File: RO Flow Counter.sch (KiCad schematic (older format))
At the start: 27 parts, among them J7 Conn_01x02, J8 Conn_01x04, K1 G5Q-1A, Q1 BC807, Q2 BC807, Q3 2N7002E

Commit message: fix rotary encoder, i2c pullup resistors, reset button placement
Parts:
- J8: value Conn_01x04 -> Programming; footprint Connector_PinHeader_2.54mm:PinHeader_1x04_P2.54mm_Vertical -> Connector_PinHeader_2.54mm:PinHeader_1x05_P2.54mm_Vertical; symbol Connector_Generic:Conn_01x04 -> Connector_Generic:Conn_01x05
- R1, R2: value 1M -> 10k
- R20: value 1k -> 10k
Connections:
- net GND: now also J8.5 (Pin_5); no longer J8.4 (Pin_4)
- new net mcu/reset: J8.4 (Pin_4)
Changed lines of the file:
@@
 F14 "SDA" B R 6675 3775 50
 F15 "RESET_LCD" O R 6675 4075 50
+F16 "reset" I R 6675 5825 50
 $EndSheet
 Wire Wire Line
@@
 P 4200 5150
 F 0 "R2" V 3993 5150 50  0000 C CNN
-F 1 "1M" V 4084 5150 50  0000 C CNN
+F 1 "10k" V 4084 5150 50  0000 C CNN
 F 2 "Resistor_SMD:R_0402_1005Metric" V 4130 5150 50  0001 C CNN
 F 3 "~" H 4200 5150 50  0001 C CNN
@@
 P 4200 4550
 F 0 "R1" V 3993 4550 50  0000 C CNN
-F 1 "1M" V 4084 4550 50  0000 C CNN
+F 1 "10k" V 4084 4550 50  0000 C CNN
 F 2 "Resistor_SMD:R_0402_1005Metric" V 4130 4550 50  0001 C CNN
 F 3 "~" H 4200 4550 50  0001 C CNN
@@
 $EndComp
 $Comp
-L Connector_Generic:Conn_01x04 J8
+L Connector_Generic:Conn_01x05 J8
 U 1 1 62E41334
-P 7750 5625
-F 0 "J8" H 7830 5617 50  0000 L CNN
-F 1 "Conn_01x04" H 7830 5526 50  0000 L CNN
-F 2 "Connector_PinHeader_2.54mm:PinHeader_1x04_P2.54mm_Vertical" H 7750 5625 50  0001 C CNN
-F 3 "~" H 7750 5625 50  0001 C CNN
-	1    7750 5625
+P 7750 5725
+F 0 "J8" H 7830 5717 50  0000 L CNN
+F 1 "Programming" H 7830 5626 50  0000 L CNN
+F 2 "Connector_PinHeader_2.54mm:PinHeader_1x05_P2.54mm_Vertical" H 7750 5725 50  0001 C CNN
+F 3 "~" H 7750 5725 50  0001 C CNN
+	1    7750 5725
 	1    0    0    -1
 $EndComp
@@
 	7225 5525 7225 5300
 Wire Wire Line
-	7550 5825 7225 5825
-Wire Wire Line
-	7225 5825 7225 6050
+	7550 5925 7225 5925
+Wire Wire Line
+	7225 5925 7225 6150
 $Comp
 L power:GND #PWR031
 U 1 1 62E44ED0
-P 7225 6050
-F 0 "#PWR031" H 7225 5800 50  0001 C CNN
-F 1 "GND" H 7230 5877 50  0000 C CNN
-F 2 "" H 7225 6050 50  0001 C CNN
-F 3 "" H 7225 6050 50  0001 C CNN
-	1    7225 6050
+P 7225 6150
+F 0 "#PWR031" H 7225 5900 50  0001 C CNN
+F 1 "GND" H 7230 5977 50  0000 C CNN
+F 2 "" H 7225 6150 50  0001 C CNN
+F 3 "" H 7225 6150 50  0001 C CNN
+	1    7225 6150
 	1    0    0    -1
 $EndComp
@@
 P 7725 2925
 F 0 "R20" V 7518 2925 50  0000 C CNN
-F 1 "1k" V 7609 2925 50  0000 C CNN
+F 1 "10k" V 7609 2925 50  0000 C CNN
 F 2 "Resistor_SMD:R_0402_1005Metric" V 7655 2925 50  0001 C CNN
 F 3 "~" H 7725 2925 50  0001 C CNN
@@
 Wire Wire Line
 	7725 3225 8125 3225
+Wire Wire Line
+	7550 5825 6675 5825
 $EndSCHEMATC

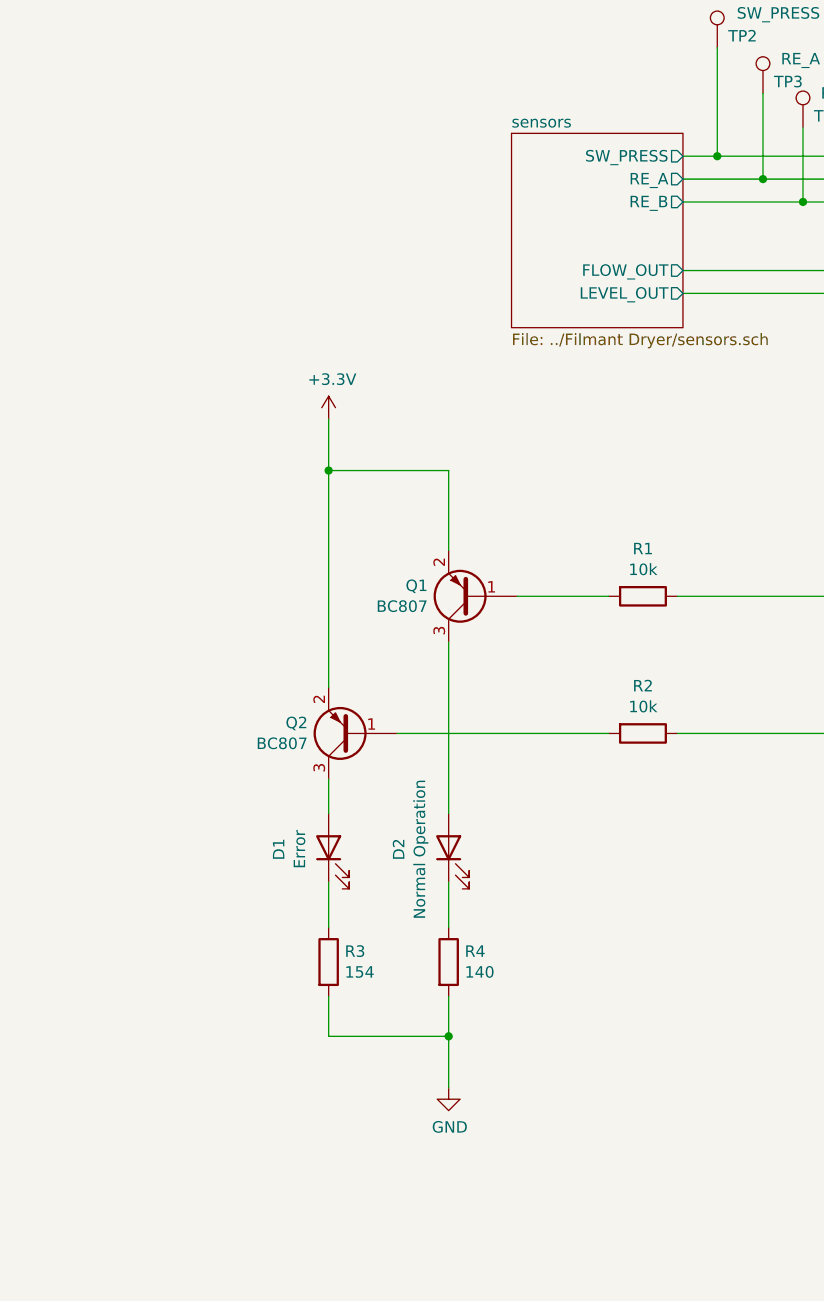
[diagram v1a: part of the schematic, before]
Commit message: use mosfet for led instead of bjt
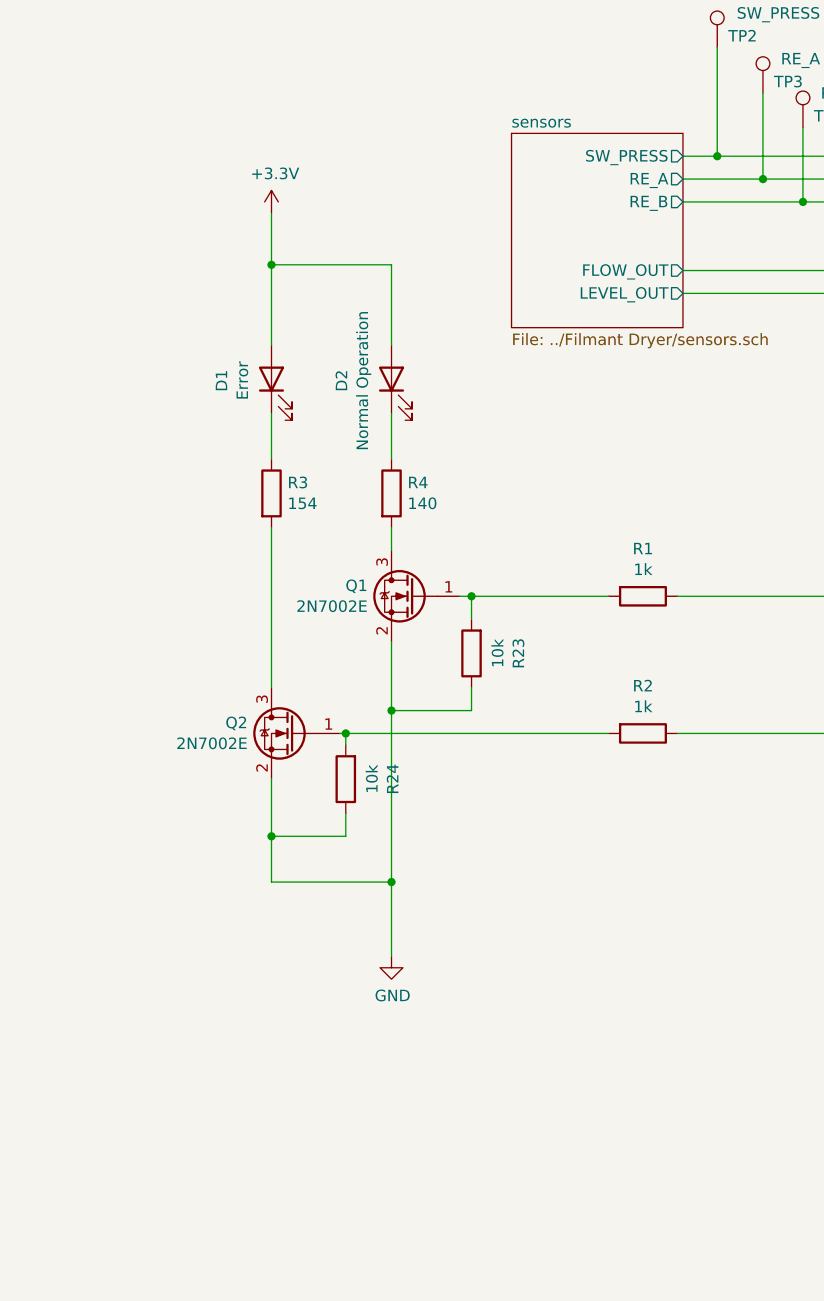
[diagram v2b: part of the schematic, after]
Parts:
- removed Q1, Q2: BC807, Package_TO_SOT_SMD:SOT-23, symbol Transistor_BJT:BC807
- added Q1, Q2: 2N7002E, Package_TO_SOT_SMD:SOT-23, symbol Transistor_FET:2N7002E
- added R23, R24: 10k, Resistor_SMD:R_0402_1005Metric, symbol Device:R
- R1, R2: value 10k -> 1k
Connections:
- net +3V3: now also D1.2 (A), D2.2 (A)
- net GND: now also Q1.2 (S), Q2.2 (S), R23.1, R24.1; no longer R3.2, R4.2
- net at R1.2: now also Q1.1 (G), R23.2
- net at R2.2: now also Q2.1 (G), R24.2
- new net: Q2.3 (D), R3.2
- new net: Q1.3 (D), R4.2
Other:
- moved on the sheet: D1, D2, R3, R4
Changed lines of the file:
@@
 L Device:LED D1
 U 1 1 62E04814
-P 2825 5650
-F 0 "D1" H 2818 5867 50  0000 C CNN
-F 1 "Error" H 2818 5776 50  0000 C CNN
-F 2 "LED_SMD:LED_0805_2012Metric" H 2825 5650 50  0001 C CNN
-F 3 "~" H 2825 5650 50  0001 C CNN
-	1    2825 5650
+P 2575 3600
+F 0 "D1" H 2568 3817 50  0000 C CNN
+F 1 "Error" H 2568 3726 50  0000 C CNN
+F 2 "LED_SMD:LED_0805_2012Metric" H 2575 3600 50  0001 C CNN
+F 3 "~" H 2575 3600 50  0001 C CNN
+	1    2575 3600
 	0    -1   -1   0
 $EndComp
@@
 L Device:LED D2
 U 1 1 62E049EE
-P 3350 5650
-F 0 "D2" H 3343 5867 50  0000 C CNN
-F 1 "Normal Operation" H 3343 5776 50  0000 C CNN
-F 2 "LED_SMD:LED_0805_2012Metric" H 3350 5650 50  0001 C CNN
-F 3 "~" H 3350 5650 50  0001 C CNN
-	1    3350 5650
+P 3100 3600
+F 0 "D2" H 3093 3817 50  0000 C CNN
+F 1 "Normal Operation" H 3093 3726 50  0000 C CNN
+F 2 "LED_SMD:LED_0805_2012Metric" H 3100 3600 50  0001 C CNN
+F 3 "~" H 3100 3600 50  0001 C CNN
+	1    3100 3600
 	0    -1   -1   0
 $EndComp
-$Comp
-L Transistor_BJT:BC807 Q1
-U 1 1 62E0B219
-P 3450 4550
-F 0 "Q1" H 3641 4504 50  0000 L CNN
-F 1 "BC807" H 3641 4595 50  0000 L CNN
-F 2 "Package_TO_SOT_SMD:SOT-23" H 3650 4475 50  0001 L CIN
-F 3 "https://www.onsemi.com/pub/Collateral/BC808-D.pdf" H 3450 4550 50  0001 L CNN
-	1    3450 4550
-	-1   0    0    1
-$EndComp
-$Comp
-L Transistor_BJT:BC807 Q2
-U 1 1 62E0CCA7
-P 2925 5150
-F 0 "Q2" H 3116 5104 50  0000 L CNN
-F 1 "BC807" H 3116 5195 50  0000 L CNN
-F 2 "Package_TO_SOT_SMD:SOT-23" H 3125 5075 50  0001 L CIN
-F 3 "https://www.onsemi.com/pub/Collateral/BC808-D.pdf" H 2925 5150 50  0001 L CNN
-	1    2925 5150
-	-1   0    0    1
-$EndComp
-Wire Wire Line
-	3350 4350 3350 4000
-Wire Wire Line
-	2825 4000 2825 4950
-Wire Wire Line
-	3350 5500 3350 4750
-Wire Wire Line
-	2825 5350 2825 5500
-Wire Wire Line
-	3350 4000 2825 4000
-Wire Wire Line
-	2825 4000 2825 3775
-Connection ~ 2825 4000
 $Comp
 L Device:R R4
 U 1 1 62E115BD
-P 3350 6150
-F 0 "R4" H 3420 6196 50  0000 L CNN
-F 1 "140" H 3420 6105 50  0000 L CNN
-F 2 "Resistor_SMD:R_0402_1005Metric" V 3280 6150 50  0001 C CNN
-F 3 "~" H 3350 6150 50  0001 C CNN
-	1    3350 6150
+P 3100 4100
+F 0 "R4" H 3170 4146 50  0000 L CNN
+F 1 "140" H 3170 4055 50  0000 L CNN
+F 2 "Resistor_SMD:R_0402_1005Metric" V 3030 4100 50  0001 C CNN
+F 3 "~" H 3100 4100 50  0001 C CNN
+	1    3100 4100
 	1    0    0    -1
 $EndComp
@@
 L Device:R R3
 U 1 1 62E11255
-P 2825 6150
-F 0 "R3" H 2895 6196 50  0000 L CNN
-F 1 "154" H 2895 6105 50  0000 L CNN
-F 2 "Resistor_SMD:R_0402_1005Metric" V 2755 6150 50  0001 C CNN
-F 3 "~" H 2825 6150 50  0001 C CNN
-	1    2825 6150
-	1    0    0    -1
-$EndComp
-Wire Wire Line
-	2825 6000 2825 5800
-Wire Wire Line
-	2825 6300 2825 6475
-Wire Wire Line
-	2825 6475 3350 6475
-Wire Wire Line
-	3350 6475 3350 6300
-Wire Wire Line
-	3350 6475 3350 6700
-Connection ~ 3350 6475
-Wire Wire Line
-	3125 5150 4050 5150
-Wire Wire Line
-	3650 4550 4050 4550
+P 2575 4100
+F 0 "R3" H 2645 4146 50  0000 L CNN
+F 1 "154" H 2645 4055 50  0000 L CNN
+F 2 "Resistor_SMD:R_0402_1005Metric" V 2505 4100 50  0001 C CNN
+F 3 "~" H 2575 4100 50  0001 C CNN
+	1    2575 4100
+	1    0    0    -1
+$EndComp
+Wire Wire Line
+	2575 3950 2575 3750
 $Comp
 L Device:R R2
@@
 P 4200 5150
 F 0 "R2" V 3993 5150 50  0000 C CNN
-F 1 "10k" V 4084 5150 50  0000 C CNN
+F 1 "1k" V 4084 5150 50  0000 C CNN
 F 2 "Resistor_SMD:R_0402_1005Metric" V 4130 5150 50  0001 C CNN
 F 3 "~" H 4200 5150 50  0001 C CNN
@@
 P 4200 4550
 F 0 "R1" V 3993 4550 50  0000 C CNN
-F 1 "10k" V 4084 4550 50  0000 C CNN
+F 1 "1k" V 4084 4550 50  0000 C CNN
 F 2 "Resistor_SMD:R_0402_1005Metric" V 4130 4550 50  0001 C CNN
 F 3 "~" H 4200 4550 50  0001 C CNN
@@
 	4350 5150 5150 5150
 Wire Wire Line
-	3350 5800 3350 6000
+	3100 3750 3100 3950
 $Comp
 L power:+3.3V #PWR01
 U 1 1 62E1866C
-P 2825 3775
-F 0 "#PWR01" H 2825 3625 50  0001 C CNN
-F 1 "+3.3V" H 2840 3948 50  0000 C CNN
-F 2 "" H 2825 3775 50  0001 C CNN
-F 3 "" H 2825 3775 50  0001 C CNN
-	1    2825 3775
-	1    0    0    -1
-$EndComp
-$Comp
-L power:GND #PWR02
-U 1 1 62E1998F
-P 3350 6700
-F 0 "#PWR02" H 3350 6450 50  0001 C CNN
-F 1 "GND" H 3355 6527 50  0000 C CNN
-F 2 "" H 3350 6700 50  0001 C CNN
-F 3 "" H 3350 6700 50  0001 C CNN
-	1    3350 6700
+P 2575 2875
+F 0 "#PWR01" H 2575 2725 50  0001 C CNN
+F 1 "+3.3V" H 2590 3048 50  0000 C CNN
+F 2 "" H 2575 2875 50  0001 C CNN
+F 3 "" H 2575 2875 50  0001 C CNN
+	1    2575 2875
 	1    0    0    -1
 $EndComp
@@
 Wire Wire Line
 	7550 5825 6675 5825
+$Comp
+L Transistor_FET:2N7002E Q1
+U 1 1 63028335
+P 3200 4550
+F 0 "Q1" H 3404 4596 50  0000 L CNN
+F 1 "2N7002E" H 3404 4505 50  0000 L CNN
+F 2 "Package_TO_SOT_SMD:SOT-23" H 3400 4475 50  0001 L CIN
+F 3 "http://www.diodes.com/assets/Datasheets/ds30376.pdf" H 3200 4550 50  0001 L CNN
+	1    3200 4550
+	-1   0    0    -1
+$EndComp
+Wire Wire Line
+	2575 3100 2575 2875
+Wire Wire Line
+	3100 3100 2575 3100
+Wire Wire Line
+	3100 3450 3100 3100
+$Comp
+L Transistor_FET:2N7002E Q2
+U 1 1 630420E5
+P 2675 5150
+F 0 "Q2" H 2879 5196 50  0000 L CNN
+F 1 "2N7002E" H 2879 5105 50  0000 L CNN
+F 2 "Package_TO_SOT_SMD:SOT-23" H 2875 5075 50  0001 L CIN
+F 3 "http://www.diodes.com/assets/Datasheets/ds30376.pdf" H 2675 5150 50  0001 L CNN
+	1    2675 5150
+	-1   0    0    -1
+$EndComp
+Wire Wire Line
+	2575 4950 2575 4250
+Wire Wire Line
+	3100 4250 3100 4350
+Wire Wire Line
+	3100 4750 3100 5050
+Wire Wire Line
+	2875 5150 2900 5150
+Wire Wire Line
+	3400 4550 3450 4550
+Wire Wire Line
+	2575 3100 2575 3450
+Connection ~ 2575 3100
+$Comp
+L Device:R R24
+U 1 1 63058845
+P 2900 5350
+F 0 "R24" V 2693 5350 50  0000 C CNN
+F 1 "10k" V 2784 5350 50  0000 C CNN
+F 2 "Resistor_SMD:R_0402_1005Metric" V 2830 5350 50  0001 C CNN
+F 3 "~" H 2900 5350 50  0001 C CNN
+	1    2900 5350
+	-1   0    0    1
+$EndComp
+$Comp
+L Device:R R23
+U 1 1 63059A80
+P 3450 4800
+F 0 "R23" V 3243 4800 50  0000 C CNN
+F 1 "10k" V 3334 4800 50  0000 C CNN
+F 2 "Resistor_SMD:R_0402_1005Metric" V 3380 4800 50  0001 C CNN
+F 3 "~" H 3450 4800 50  0001 C CNN
+	1    3450 4800
+	-1   0    0    1
+$EndComp
+Wire Wire Line
+	3450 4650 3450 4550
+Connection ~ 3450 4550
+Wire Wire Line
+	3450 4550 4050 4550
+Wire Wire Line
+	3450 4950 3450 5050
+Wire Wire Line
+	3450 5050 3100 5050
+Wire Wire Line
+	2900 5200 2900 5150
+Connection ~ 2900 5150
+Wire Wire Line
+	2900 5150 4050 5150
+Wire Wire Line
+	2900 5500 2900 5600
+Wire Wire Line
+	2900 5600 2575 5600
+Wire Wire Line
+	2575 5350 2575 5600
+Wire Wire Line
+	2575 5600 2575 5800
+Wire Wire Line
+	2575 5800 3100 5800
+Wire Wire Line
+	3100 5800 3100 5050
+Connection ~ 2575 5600
+Connection ~ 3100 5050
+Wire Wire Line
+	3100 5800 3100 6125
+Connection ~ 3100 5800
+$Comp
+L power:GND #PWR02
+U 1 1 63073E68
+P 3100 6125
+F 0 "#PWR02" H 3100 5875 50  0001 C CNN
+F 1 "GND" H 3105 5952 50  0000 C CNN
+F 2 "" H 3100 6125 50  0001 C CNN
+F 3 "" H 3100 6125 50  0001 C CNN
+	1    3100 6125
+	1    0    0    -1
+$EndComp
 $EndSCHEMATC

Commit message: finish v2
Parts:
- added D6: WiFi, LED_SMD:LED_0805_2012Metric, symbol Device:LED
- added Q5: 2N7002E, Package_TO_SOT_SMD:SOT-23, symbol Transistor_FET:2N7002E
- added R25: 154, Resistor_SMD:R_0402_1005Metric, symbol Device:R
- added R26: 1k, Resistor_SMD:R_0402_1005Metric, symbol Device:R
- added R27: 10k, Resistor_SMD:R_0402_1005Metric, symbol Device:R
- J7: footprint Connector_Wire:SolderWire-0.75sqmm_1x02_P7mm_D1.25mm_OD3.5mm -> Connector_Wire:SolderWire-2.5sqmm_1x02_P8.8mm_D2.4mm_OD4.4mm
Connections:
- net +3V3: now also D6.2 (A)
- net GND: now also Q5.2 (S), R27.1
- new net: D6.1 (K), R25.1
- new net: Q5.3 (D), R25.2
- new net: Q5.1 (G), R26.2, R27.2
- new net mcu/LED_WIFI: R26.1
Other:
- moved on the sheet: R23, R24
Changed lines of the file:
@@
 F15 "RESET_LCD" O R 6675 4075 50
 F16 "reset" I R 6675 5825 50
+F17 "LED_WIFI" O L 5150 5850 50
 $EndSheet
 Wire Wire Line
@@
 L power:+3.3V #PWR01
 U 1 1 62E1866C
-P 2575 2875
-F 0 "#PWR01" H 2575 2725 50  0001 C CNN
-F 1 "+3.3V" H 2590 3048 50  0000 C CNN
-F 2 "" H 2575 2875 50  0001 C CNN
-F 3 "" H 2575 2875 50  0001 C CNN
-	1    2575 2875
+P 2075 2875
+F 0 "#PWR01" H 2075 2725 50  0001 C CNN
+F 1 "+3.3V" H 2090 3048 50  0000 C CNN
+F 2 "" H 2075 2875 50  0001 C CNN
+F 3 "" H 2075 2875 50  0001 C CNN
+	1    2075 2875
 	1    0    0    -1
 $EndComp
@@
 F 0 "J7" H 9205 2092 50  0000 L CNN
 F 1 "Conn_01x02" H 9205 2001 50  0000 L CNN
-F 2 "Connector_Wire:SolderWire-0.75sqmm_1x02_P7mm_D1.25mm_OD3.5mm" H 9125 2100 50  0001 C CNN
+F 2 "Connector_Wire:SolderWire-2.5sqmm_1x02_P8.8mm_D2.4mm_OD4.4mm" H 9125 2100 50  0001 C CNN
 F 3 "~" H 9125 2100 50  0001 C CNN
 	1    9125 2100
@@
 $EndComp
 Wire Wire Line
-	2575 3100 2575 2875
+	2075 3100 2075 2875
 Wire Wire Line
 	3100 3100 2575 3100
@@
 	2875 5150 2900 5150
 Wire Wire Line
-	3400 4550 3450 4550
+	3400 4550 3425 4550
 Wire Wire Line
 	2575 3100 2575 3450
@@
 L Device:R R24
 U 1 1 63058845
-P 2900 5350
-F 0 "R24" V 2693 5350 50  0000 C CNN
-F 1 "10k" V 2784 5350 50  0000 C CNN
-F 2 "Resistor_SMD:R_0402_1005Metric" V 2830 5350 50  0001 C CNN
-F 3 "~" H 2900 5350 50  0001 C CNN
-	1    2900 5350
+P 2900 5400
+F 0 "R24" V 2693 5400 50  0000 C CNN
+F 1 "10k" V 2784 5400 50  0000 C CNN
+F 2 "Resistor_SMD:R_0402_1005Metric" V 2830 5400 50  0001 C CNN
+F 3 "~" H 2900 5400 50  0001 C CNN
+	1    2900 5400
 	-1   0    0    1
 $EndComp
@@
 L Device:R R23
 U 1 1 63059A80
-P 3450 4800
-F 0 "R23" V 3243 4800 50  0000 C CNN
-F 1 "10k" V 3334 4800 50  0000 C CNN
-F 2 "Resistor_SMD:R_0402_1005Metric" V 3380 4800 50  0001 C CNN
-F 3 "~" H 3450 4800 50  0001 C CNN
-	1    3450 4800
+P 3425 4800
+F 0 "R23" V 3218 4800 50  0000 C CNN
+F 1 "10k" V 3309 4800 50  0000 C CNN
+F 2 "Resistor_SMD:R_0402_1005Metric" V 3355 4800 50  0001 C CNN
+F 3 "~" H 3425 4800 50  0001 C CNN
+	1    3425 4800
 	-1   0    0    1
 $EndComp
 Wire Wire Line
-	3450 4650 3450 4550
-Connection ~ 3450 4550
-Wire Wire Line
-	3450 4550 4050 4550
-Wire Wire Line
-	3450 4950 3450 5050
-Wire Wire Line
-	3450 5050 3100 5050
-Wire Wire Line
-	2900 5200 2900 5150
+	3425 4650 3425 4550
+Connection ~ 3425 4550
+Wire Wire Line
+	3425 4550 4050 4550
+Wire Wire Line
+	3425 4950 3425 5050
+Wire Wire Line
+	3425 5050 3100 5050
+Wire Wire Line
+	2900 5250 2900 5150
 Connection ~ 2900 5150
 Wire Wire Line
 	2900 5150 4050 5150
 Wire Wire Line
-	2900 5500 2900 5600
-Wire Wire Line
-	2900 5600 2575 5600
-Wire Wire Line
-	2575 5350 2575 5600
-Wire Wire Line
-	2575 5600 2575 5800
+	2900 5550 2900 5650
+Wire Wire Line
+	2900 5650 2575 5650
+Wire Wire Line
+	2575 5350 2575 5650
+Wire Wire Line
+	2575 5650 2575 5800
 Wire Wire Line
 	2575 5800 3100 5800
 Wire Wire Line
 	3100 5800 3100 5050
-Connection ~ 2575 5600
+Connection ~ 2575 5650
 Connection ~ 3100 5050
-Wire Wire Line
-	3100 5800 3100 6125
-Connection ~ 3100 5800
+$Comp
+L Device:LED D6
+U 1 1 63052445
+P 2075 3600
+F 0 "D6" H 2068 3817 50  0000 C CNN
+F 1 "WiFi" H 2068 3726 50  0000 C CNN
+F 2 "LED_SMD:LED_0805_2012Metric" H 2075 3600 50  0001 C CNN
+F 3 "~" H 2075 3600 50  0001 C CNN
+	1    2075 3600
+	0    -1   -1   0
+$EndComp
+$Comp
+L Device:R R25
+U 1 1 6305244B
+P 2075 4100
+F 0 "R25" H 2145 4146 50  0000 L CNN
+F 1 "154" H 2145 4055 50  0000 L CNN
+F 2 "Resistor_SMD:R_0402_1005Metric" V 2005 4100 50  0001 C CNN
+F 3 "~" H 2075 4100 50  0001 C CNN
+	1    2075 4100
+	1    0    0    -1
+$EndComp
+Wire Wire Line
+	2075 3950 2075 3750
+$Comp
+L Transistor_FET:2N7002E Q5
+U 1 1 63052452
+P 2175 5850
+F 0 "Q5" H 2379 5896 50  0000 L CNN
+F 1 "2N7002E" H 2379 5805 50  0000 L CNN
+F 2 "Package_TO_SOT_SMD:SOT-23" H 2375 5775 50  0001 L CIN
+F 3 "http://www.diodes.com/assets/Datasheets/ds30376.pdf" H 2175 5850 50  0001 L CNN
+	1    2175 5850
+	-1   0    0    -1
+$EndComp
+Wire Wire Line
+	2375 5850 2400 5850
+Wire Wire Line
+	2075 3100 2075 3450
+$Comp
+L Device:R R27
+U 1 1 6305245B
+P 2400 6100
+F 0 "R27" V 2193 6100 50  0000 C CNN
+F 1 "10k" V 2284 6100 50  0000 C CNN
+F 2 "Resistor_SMD:R_0402_1005Metric" V 2330 6100 50  0001 C CNN
+F 3 "~" H 2400 6100 50  0001 C CNN
+	1    2400 6100
+	-1   0    0    1
+$EndComp
+Wire Wire Line
+	2400 5950 2400 5850
+Connection ~ 2400 5850
+Wire Wire Line
+	2400 6250 2400 6350
+Wire Wire Line
+	2400 6350 2075 6350
+Wire Wire Line
+	2075 6050 2075 6350
+Wire Wire Line
+	2075 6350 2075 6500
+Connection ~ 2075 6350
+Wire Wire Line
+	2075 4250 2075 5650
+Wire Wire Line
+	2075 3100 2575 3100
+Connection ~ 2075 3100
 $Comp
 L power:GND #PWR02
 U 1 1 63073E68
-P 3100 6125
-F 0 "#PWR02" H 3100 5875 50  0001 C CNN
-F 1 "GND" H 3105 5952 50  0000 C CNN
-F 2 "" H 3100 6125 50  0001 C CNN
-F 3 "" H 3100 6125 50  0001 C CNN
-	1    3100 6125
-	1    0    0    -1
-$EndComp
+P 3100 6725
+F 0 "#PWR02" H 3100 6475 50  0001 C CNN
+F 1 "GND" H 3105 6552 50  0000 C CNN
+F 2 "" H 3100 6725 50  0001 C CNN
+F 3 "" H 3100 6725 50  0001 C CNN
+	1    3100 6725
+	1    0    0    -1
+$EndComp
+Wire Wire Line
+	3100 5800 3100 6500
+Connection ~ 3100 5800
+Wire Wire Line
+	2075 6500 3100 6500
+Connection ~ 3100 6500
+Wire Wire Line
+	3100 6500 3100 6725
+$Comp
+L Device:R R26
+U 1 1 6306EC2A
+P 4225 5850
+F 0 "R26" V 4018 5850 50  0000 C CNN
+F 1 "1k" V 4109 5850 50  0000 C CNN
+F 2 "Resistor_SMD:R_0402_1005Metric" V 4155 5850 50  0001 C CNN
+F 3 "~" H 4225 5850 50  0001 C CNN
+	1    4225 5850
+	0    1    1    0
+$EndComp
+Wire Wire Line
+	2400 5850 4075 5850
+Wire Wire Line
+	4375 5850 5150 5850
 $EndSCHEMATC

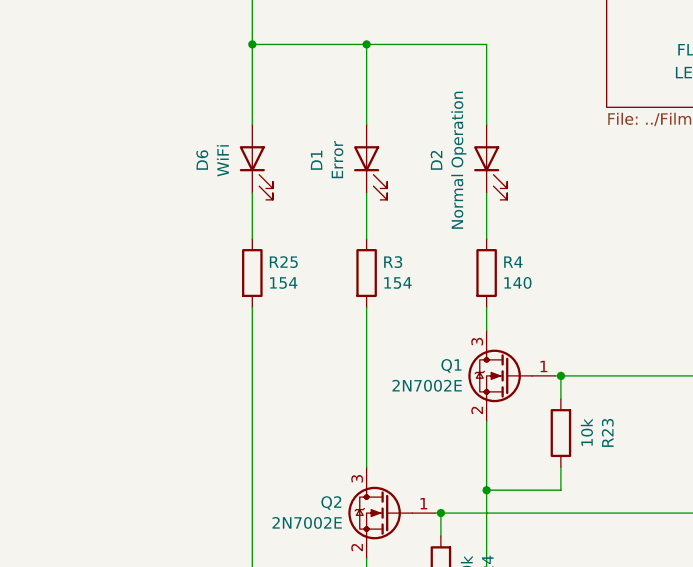
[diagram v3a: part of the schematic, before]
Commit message: fix ro GND pad
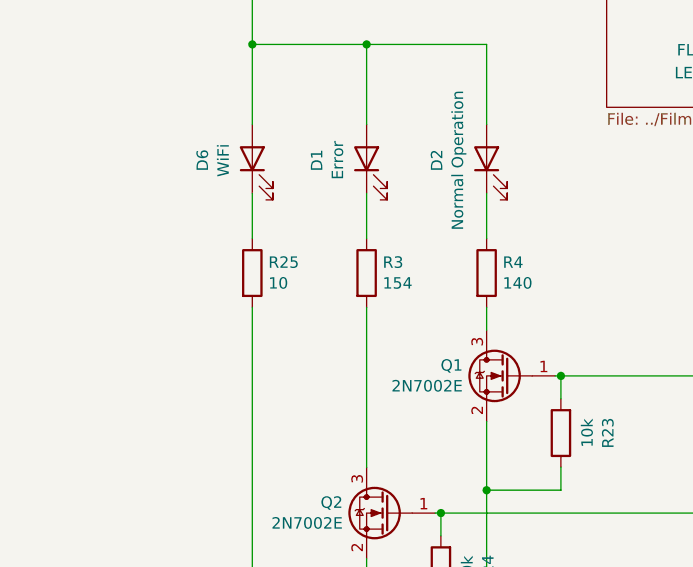
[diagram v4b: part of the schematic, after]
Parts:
- R25: value 154 -> 10
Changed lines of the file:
@@
 P 2075 4100
 F 0 "R25" H 2145 4146 50  0000 L CNN
-F 1 "154" H 2145 4055 50  0000 L CNN
+F 1 "10" H 2145 4055 50  0000 L CNN
 F 2 "Resistor_SMD:R_0402_1005Metric" V 2005 4100 50  0001 C CNN
 F 3 "~" H 2075 4100 50  0001 C CNN
